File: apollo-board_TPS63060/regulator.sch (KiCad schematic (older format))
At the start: 44 parts, among them J11 Conn_01x04_Male, Q10 2N7002A, Q11 2N7002A, Q13 DMP2035UVT, Q14 DMP2035UVT, Q5 DMP2035UVT, Q9 2N7002A, U6 TPS63060, U9 TPS63060

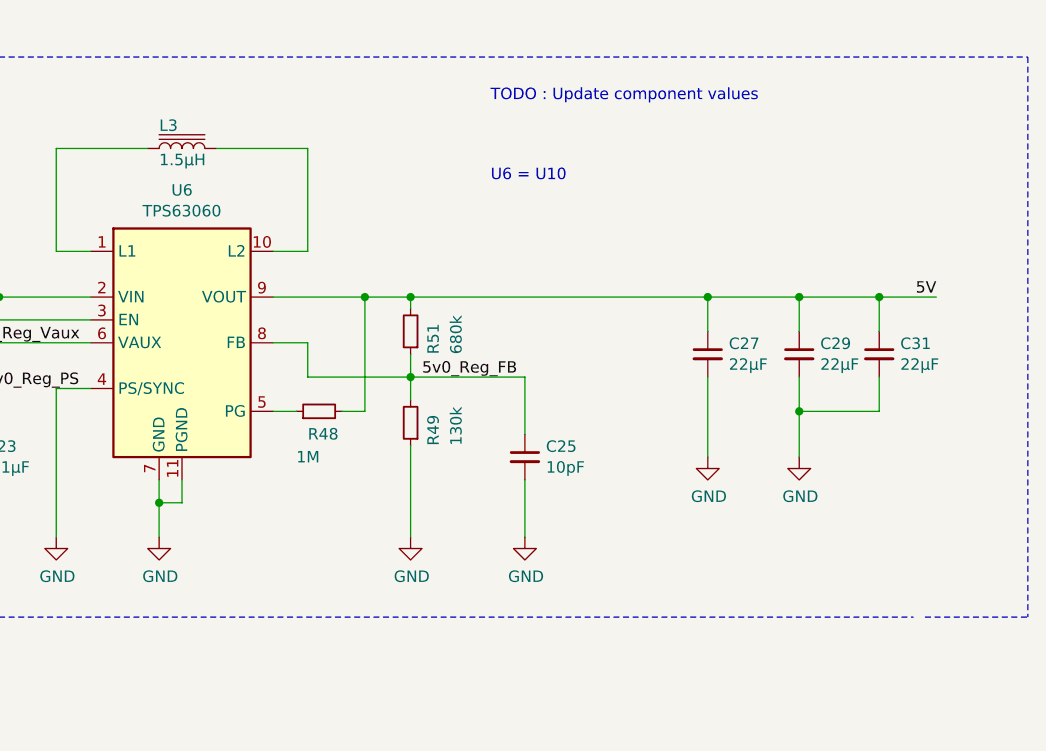
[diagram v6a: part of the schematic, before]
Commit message: Update 22µF 0805 and 10pF 0603 capacitors
+ Silk Ref. Des.
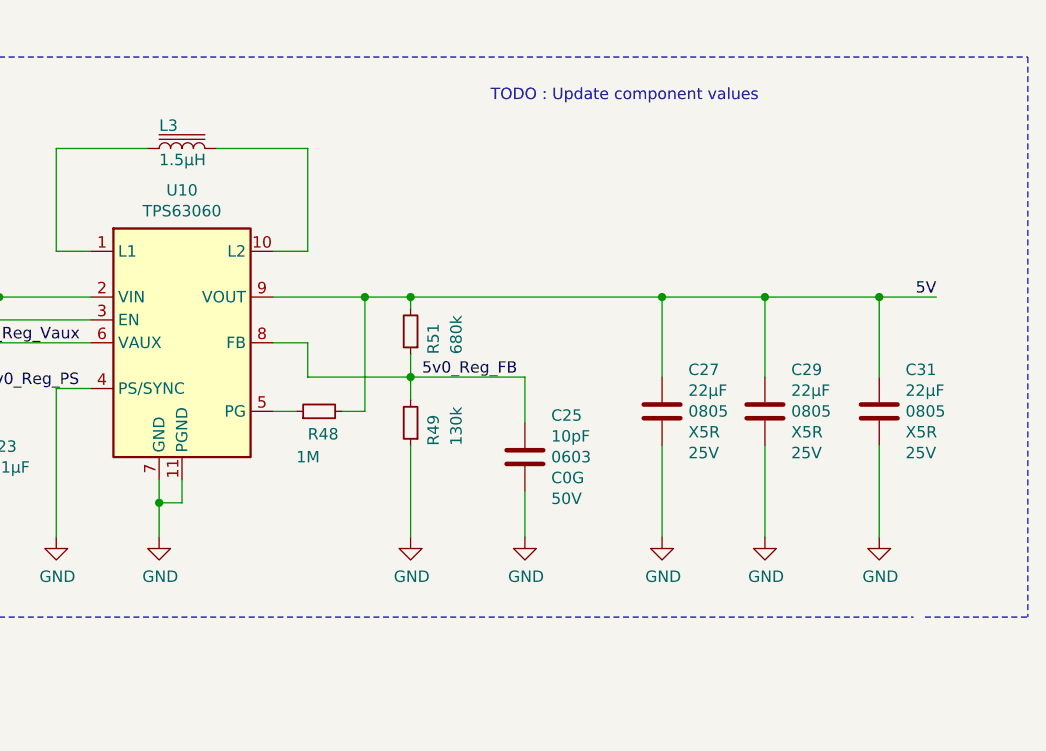
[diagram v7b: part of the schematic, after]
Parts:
- removed C25: 10pF, Capacitor_SMD:C_0603_1608Metric, symbol Device:C_Small
- removed C27, C29, C31: 22μF, Capacitor_SMD:C_0805_2012Metric, symbol Device:C_Small
- added C25: CC0603JRNPO9BN100, Capacitor_SMD:C_0603_1608Metric, symbol cc0603jrnpo9bn100:CC0603JRNPO9BN100
- added C27, C29, C31: CL21A226MAQNNNE, Capacitor_SMD:C_0805_2012Metric, symbol cl21a226maqnnne:CL21A226MAQNNNE
- renumbered U6 to U10
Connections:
- net 5V: now also C27.1, C29.1, C31.1
- net 5v0_Reg_FB: now also C25.1
- net GND: now also C25.2, C27.2, C29.2, C31.2
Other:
- note removed: "U6 = U10"

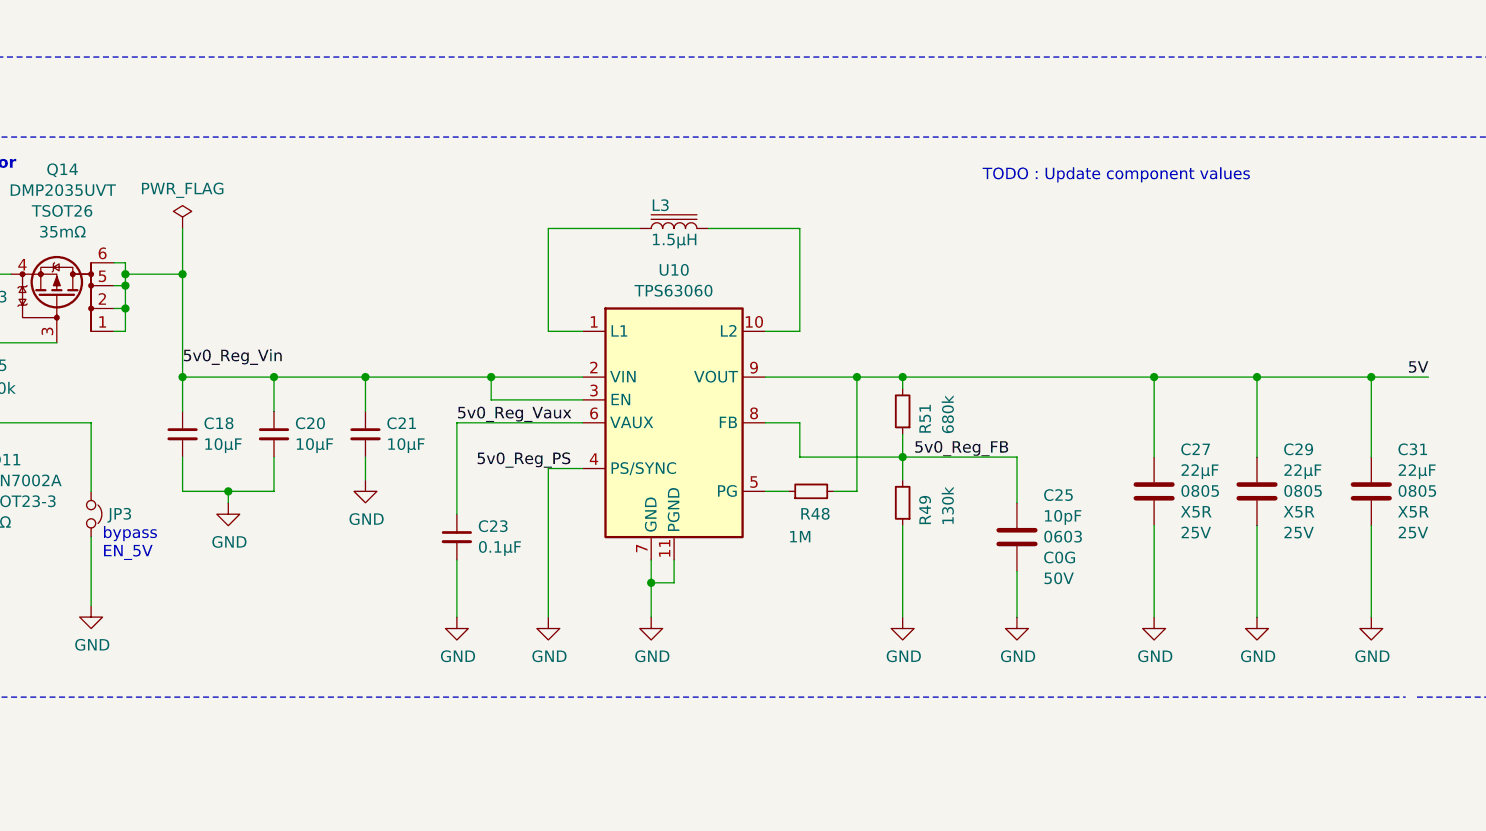
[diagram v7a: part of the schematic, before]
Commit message: Update 10µF 0805 and 100nF 0603 capacitors
+ silk Ref. Des.
Rem. : Apollo Logo and name on Silkscreen Bottom seem to be lost.
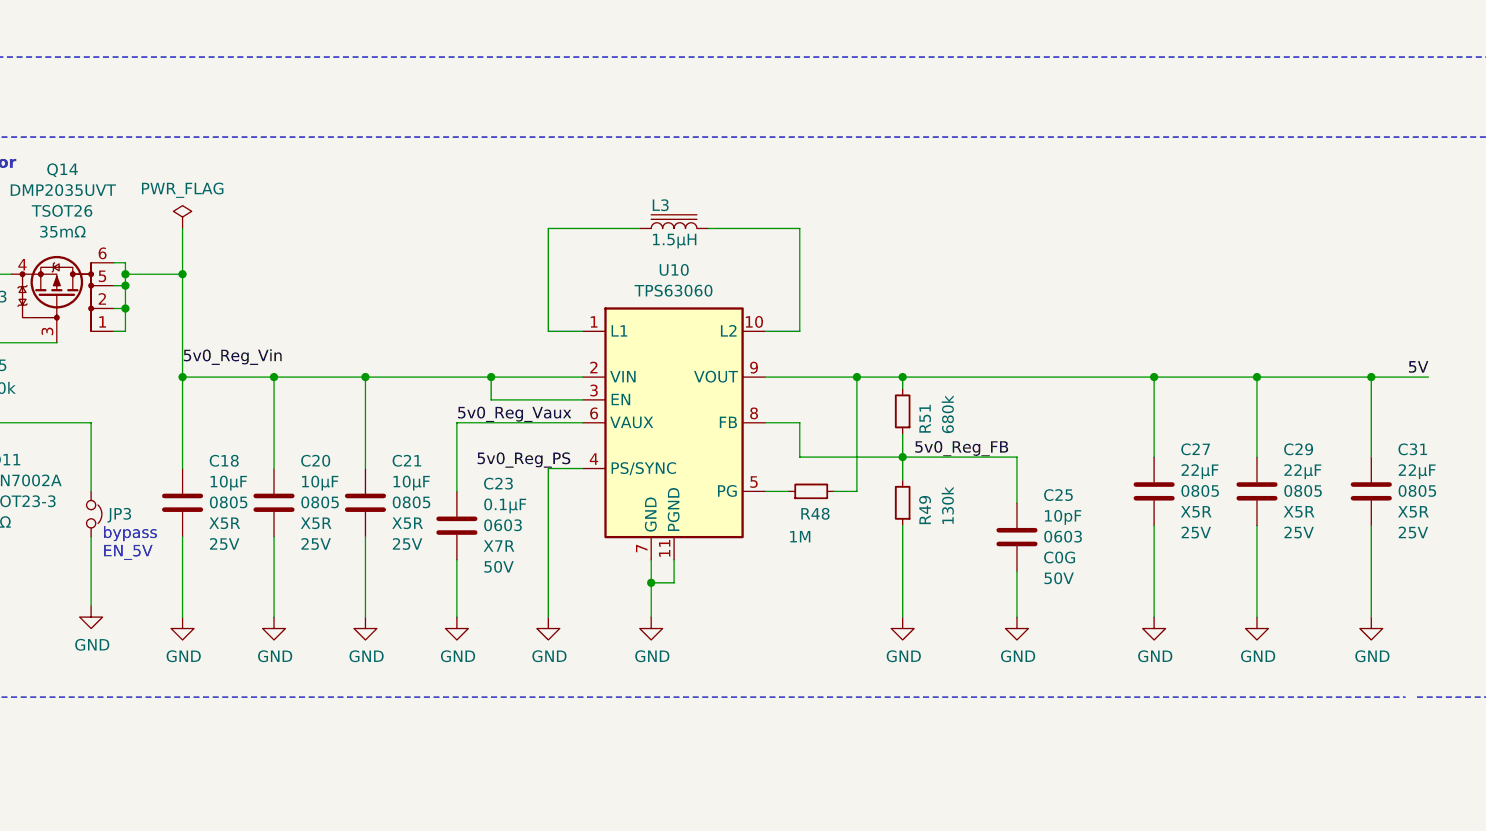
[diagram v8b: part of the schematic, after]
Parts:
- removed C18, C20, C21: 10μF, Capacitor_SMD:C_0805_2012Metric, symbol Device:C_Small
- removed C23: 0.1µF, Capacitor_SMD:C_0603_1608Metric, symbol Device:C_Small
- added C18, C20, C21: CL21A106KAYNNNE, Capacitor_SMD:C_0805_2012Metric, symbol cl21a106kaynnne:CL21A106KAYNNNE
- added C23: CL10B104KB8NNNC, Capacitor_SMD:C_0603_1608Metric, symbol cl10b104kb8nnnc:CL10B104KB8NNNC
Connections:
- net 5v0_Reg_Vaux: now also C23.1
- net 5v0_Reg_Vin: now also C18.1, C20.1, C21.1
- net GND: now also C18.2, C20.2, C21.2, C23.2
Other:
- note removed: "TODO : Update component values"
